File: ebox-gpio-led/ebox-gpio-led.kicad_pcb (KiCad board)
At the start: 2 copper layers, 45 x 75 mm, 26 parts, among them J1 xconch_pinheader_2x40, J2 xconch_pinsocket_2x40

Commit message: update some documents
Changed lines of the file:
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@@
     (thickness 1.6)
     (drawings 48)
-    (tracks 446)
+    (tracks 445)
     (zones 0)
     (modules 26)
@@
     (34 B.Paste user)
     (35 F.Paste user)
-    (36 B.SilkS user hide)
-    (37 F.SilkS user hide)
+    (36 B.SilkS user)
+    (37 F.SilkS user)
     (38 B.Mask user)
     (39 F.Mask user)
@@
     (46 B.CrtYd user)
     (47 F.CrtYd user)
-    (48 B.Fab user hide)
-    (49 F.Fab user hide)
+    (48 B.Fab user)
+    (49 F.Fab user)
   )
   (setup
-    (last_trace_width 0.125)
+    (last_trace_width 0.25)
     (user_trace_width 0.125)
     (user_trace_width 0.25)
@@
     (tags resistor)
     (attr smd)
-    (fp_text reference R1 (at -0.1205 -1.143 180) (layer B.SilkS)
+    (fp_text reference R1 (at 0.1205 1.143 180) (layer B.SilkS)
       (effects (font (size 1 1) (thickness 0.15)) (justify mirror))
     )
@@
     (tags resistor)
     (attr smd)
-    (fp_text reference R2 (at 0.0065 -1.143 180) (layer B.SilkS)
+    (fp_text reference R2 (at 0.0065 1.143 180) (layer B.SilkS)
       (effects (font (size 1 1) (thickness 0.15)) (justify mirror))
     )
@@
     (tags resistor)
     (attr smd)
-    (fp_text reference R3 (at 0 -1.143 180) (layer B.SilkS)
+    (fp_text reference R3 (at 0 1.143 180) (layer B.SilkS)
       (effects (font (size 1 1) (thickness 0.15)) (justify mirror))
     )
@@
     (tags resistor)
     (attr smd)
-    (fp_text reference R4 (at 0 -1.143 180) (layer B.SilkS)
+    (fp_text reference R4 (at 0 1.143 180) (layer B.SilkS)
       (effects (font (size 1 1) (thickness 0.15)) (justify mirror))
     )
@@
     (tags resistor)
     (attr smd)
-    (fp_text reference R5 (at 0 -1.143 180) (layer B.SilkS)
+    (fp_text reference R5 (at 0 1.143 180) (layer B.SilkS)
       (effects (font (size 1 1) (thickness 0.15)) (justify mirror))
     )
@@
     (tags resistor)
     (attr smd)
-    (fp_text reference R6 (at 0 -1.143 180) (layer B.SilkS)
+    (fp_text reference R6 (at 0.1205 1.143 180) (layer B.SilkS)
       (effects (font (size 1 1) (thickness 0.15)) (justify mirror))
     )
@@
     (tags resistor)
     (attr smd)
-    (fp_text reference R7 (at -0.1205 -1.143 180) (layer B.SilkS)
+    (fp_text reference R7 (at 0.1205 1.143 180) (layer B.SilkS)
       (effects (font (size 1 1) (thickness 0.15)) (justify mirror))
     )
@@
     (tags resistor)
     (attr smd)
-    (fp_text reference R8 (at 0.0065 -1.143 180) (layer B.SilkS)
+    (fp_text reference R8 (at 0.0065 1.143 180) (layer B.SilkS)
       (effects (font (size 1 1) (thickness 0.15)) (justify mirror))
     )
@@
     (tags resistor)
     (attr smd)
-    (fp_text reference R9 (at 0.0065 -1.143 180) (layer B.SilkS)
+    (fp_text reference R9 (at 0.0065 1.143 180) (layer B.SilkS)
       (effects (font (size 1 1) (thickness 0.15)) (justify mirror))
     )
@@
     (tags resistor)
     (attr smd)
-    (fp_text reference R10 (at -0.5015 -1.143 180) (layer B.SilkS)
+    (fp_text reference R10 (at 0.3745 1.143 180) (layer B.SilkS)
       (effects (font (size 1 1) (thickness 0.15)) (justify mirror))
     )
@@
   (segment (start 20.7 21.625) (end 22 21.625) (width 0.25) (layer B.Cu) (net 7) (status 10))
   (via (at 22.098 21.59) (size 0.4) (drill 0.2) (layers F.Cu B.Cu) (net 7))
-  (segment (start 4.445 15.875) (end 7.874 15.875) (width 0.25) (layer F.Cu) (net 33))
+  (segment (start 4.445 15.875) (end 7.747 15.875) (width 0.25) (layer F.Cu) (net 33))
+  (segment (start 7.747 15.875) (end 16.256 24.384) (width 0.25) (layer F.Cu) (net 33))
   (segment (start 16.256 24.384) (end 16.256 35.291) (width 0.25) (layer F.Cu) (net 33))
-  (segment (start 7.874 15.875) (end 7.874 16.002) (width 0.25) (layer F.Cu) (net 33))
-  (segment (start 7.874 16.002) (end 16.256 24.384) (width 0.25) (layer F.Cu) (net 33))
   (segment (start 16.256 35.291) (end 19.1 38.135) (width 0.25) (layer F.Cu) (net 33))
   (segment (start 19.1 38.135) (end 20.55 38.135) (width 0.25) (layer F.Cu) (net 33))

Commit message: update ebox
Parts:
- J2: footprint xconch:xconch_pinsocket_2x40 -> xconch_pinsocket_2x40

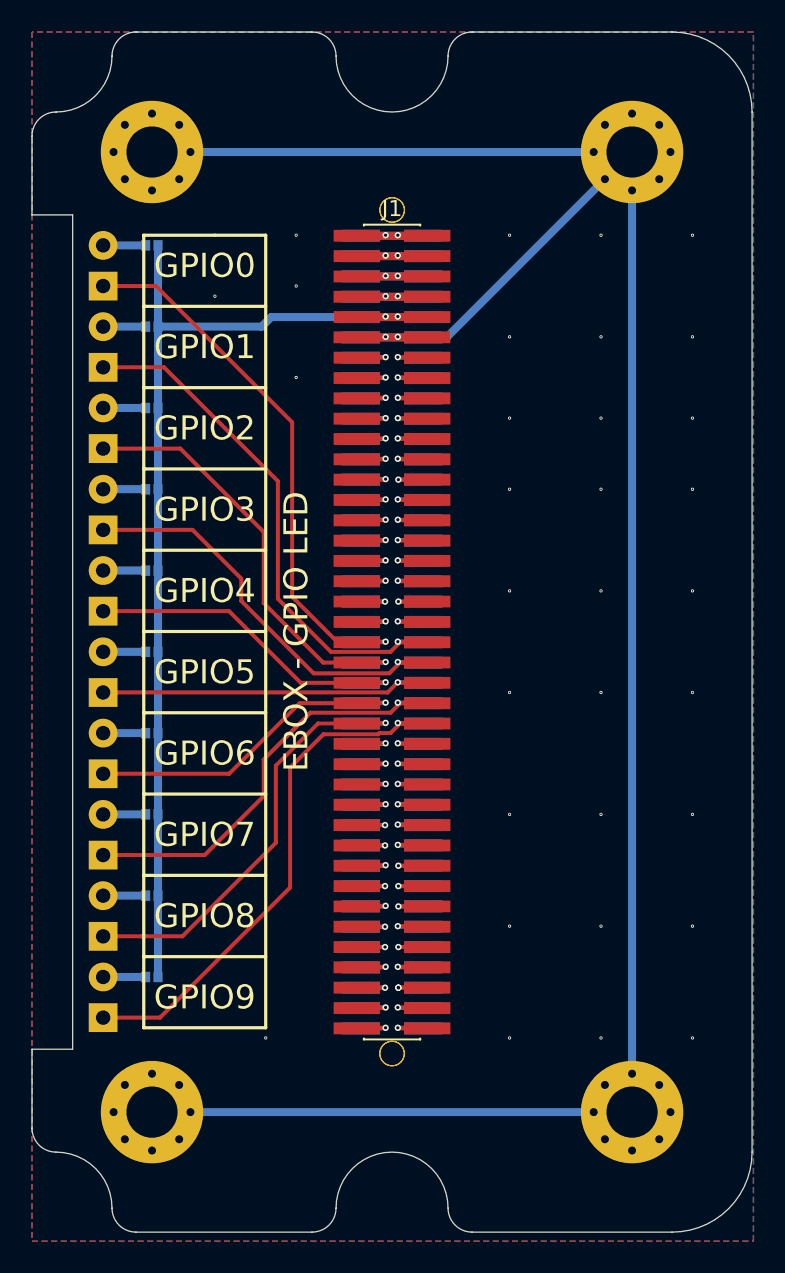
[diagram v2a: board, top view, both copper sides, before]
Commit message: add led extended box
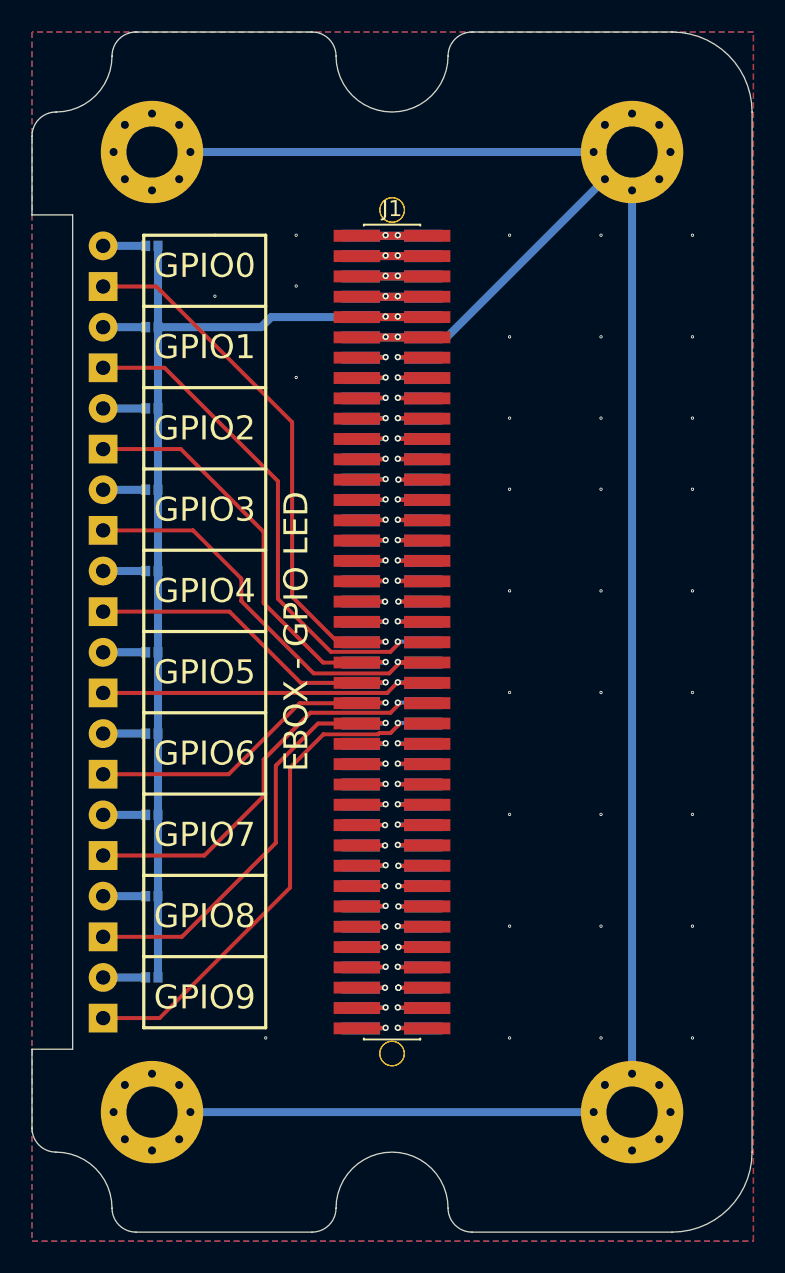
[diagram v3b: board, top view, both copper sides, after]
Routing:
- net /VCC_IO: track 66.3 -> 112.0 mm
- net /GPIO1: track 35.0 -> 32.1 mm
- net /GPIO7: track 28.3 -> 25.4 mm
- net /GPIO9: track 35.1 -> 32.2 mm

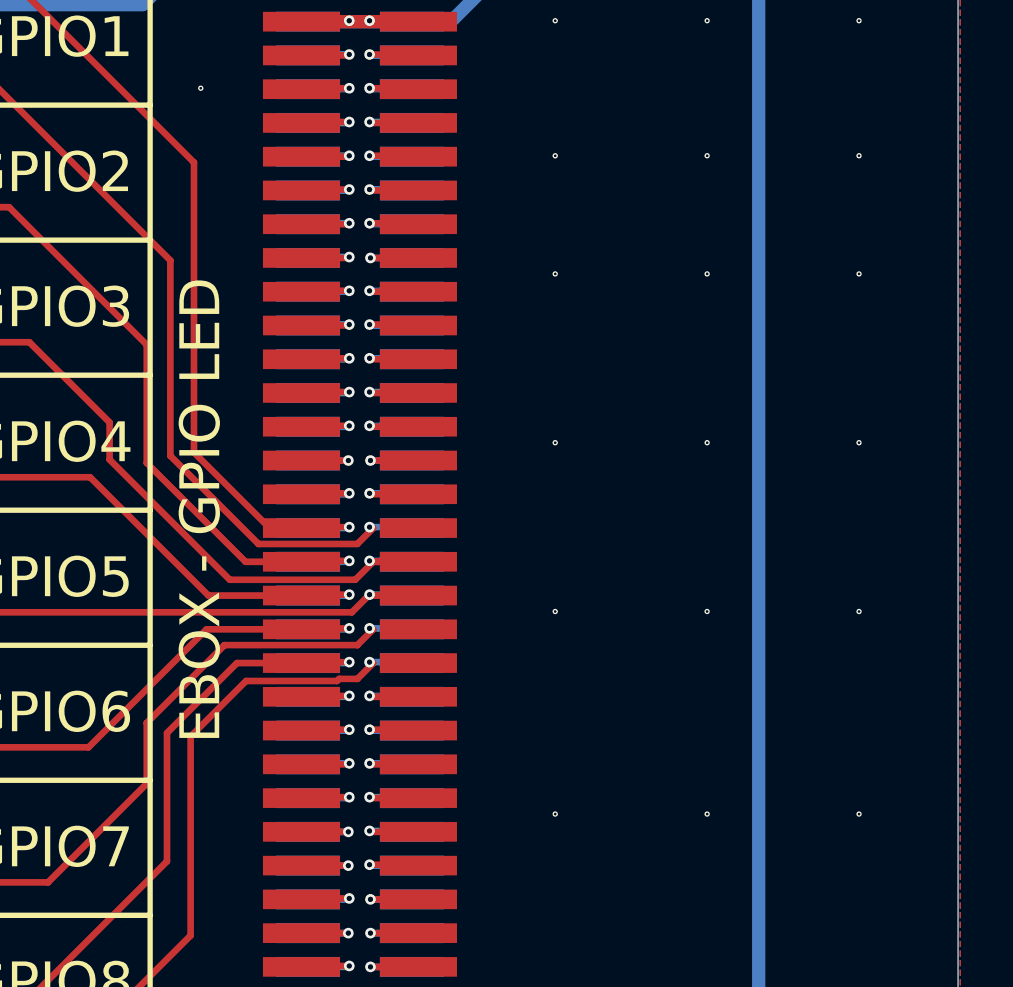
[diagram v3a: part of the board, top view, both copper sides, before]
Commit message: add logo for some pcb
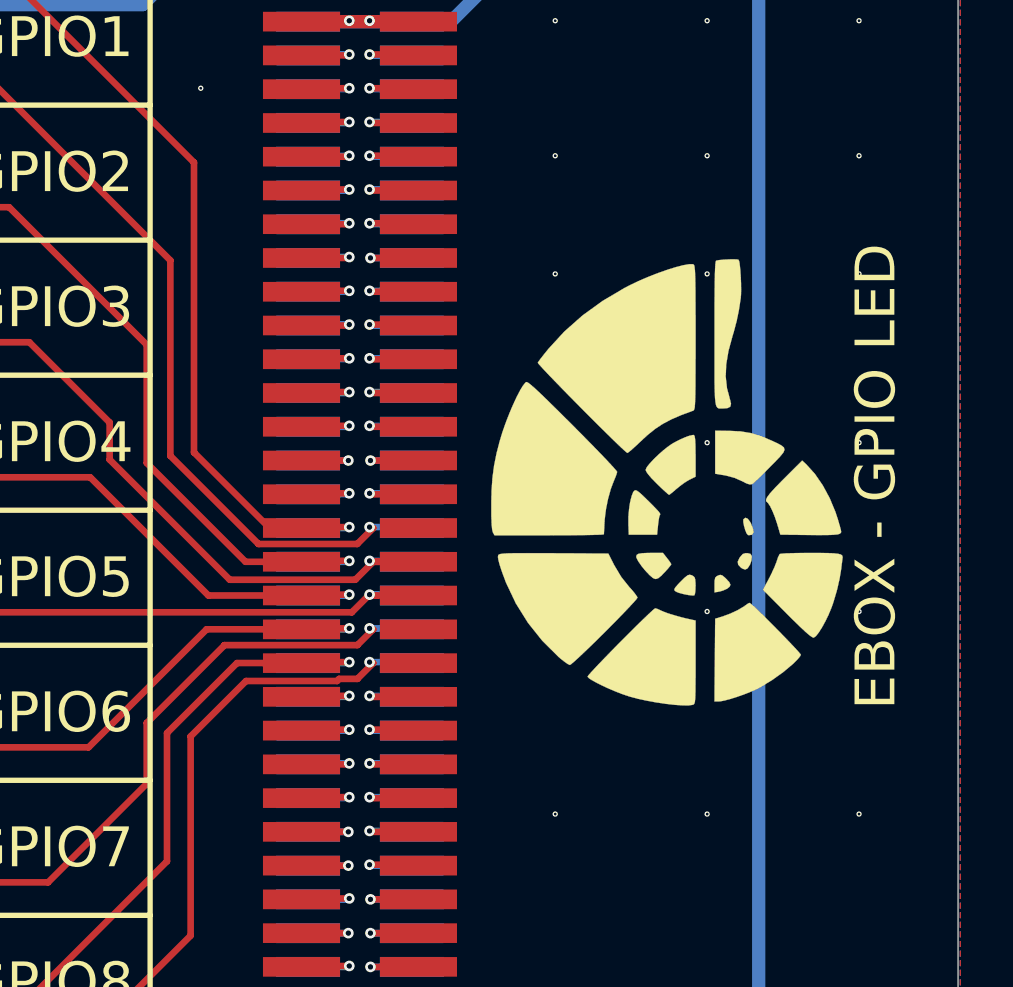
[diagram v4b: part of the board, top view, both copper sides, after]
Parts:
- added ?: , xconch:xconch_logo, F.Cu at (35.6, 38.7)
